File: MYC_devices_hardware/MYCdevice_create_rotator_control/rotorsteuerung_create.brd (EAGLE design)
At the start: 76.2 x 54.3 mm, 52 parts, among them IC1 MEGA8-P, IC3 7805T, K1 RT424012, K2 RT424012, K3 RT424012, Q1 20MHz, T1 BC547, T2 BC547, T3 BC547

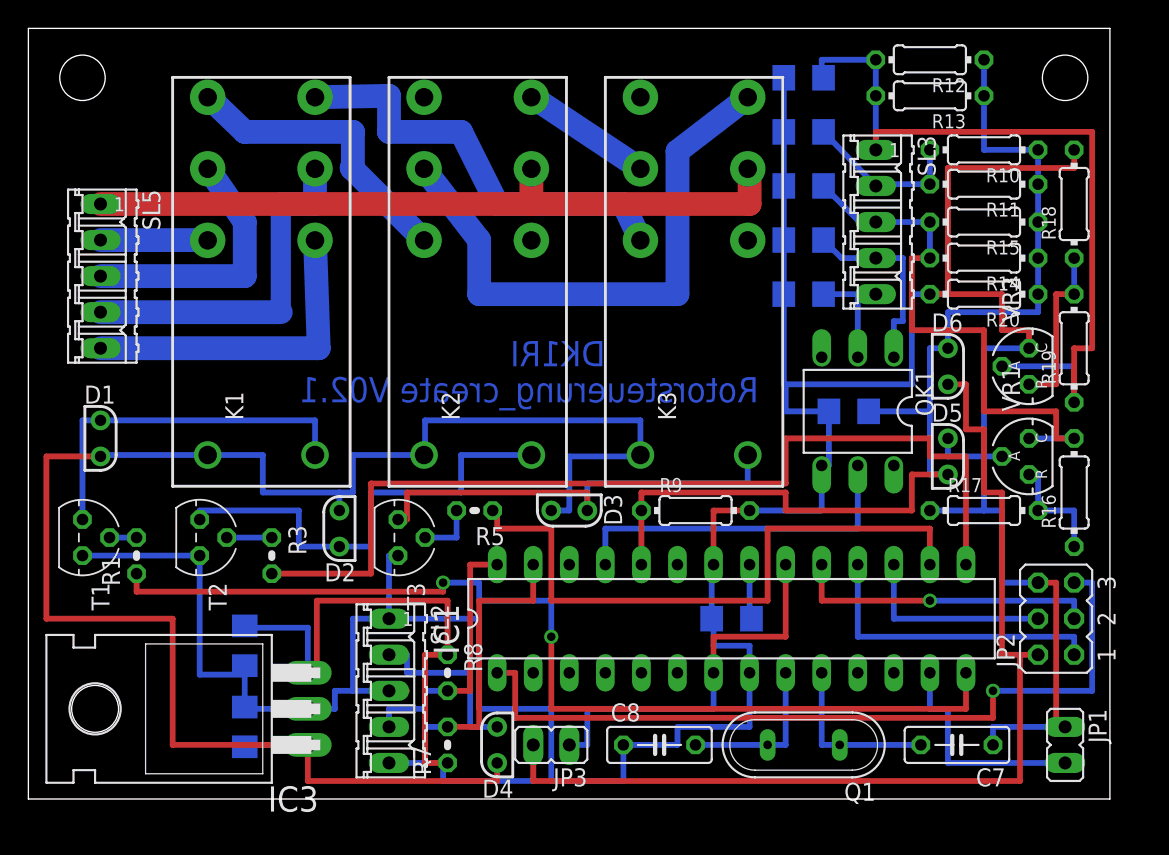
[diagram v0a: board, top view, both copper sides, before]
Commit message: new board. firmware with correction of nonlinearity and other
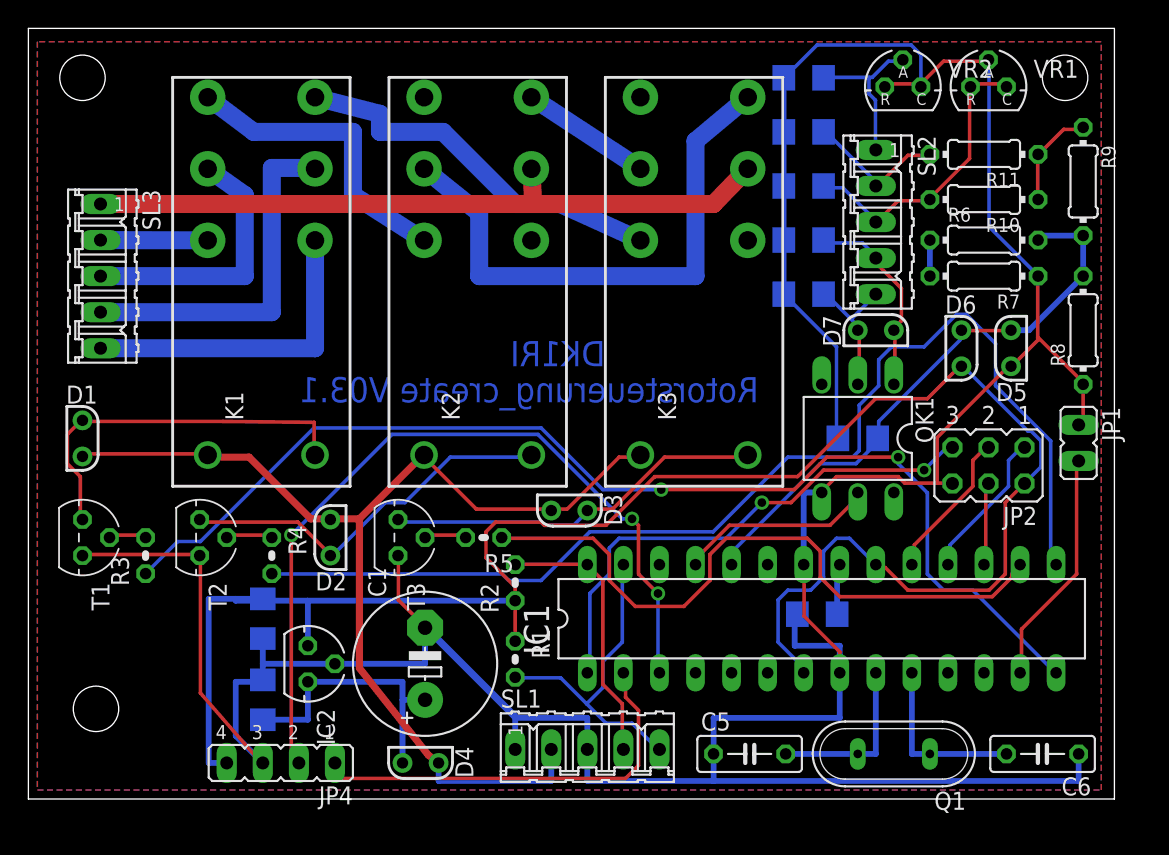
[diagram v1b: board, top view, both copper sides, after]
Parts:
- removed C13, C14, C15: 22u, resistor:C1206
- removed IC3: 7805T, linear:TO220H
- removed JP3: Power, jumper:JP1
- removed R12: 15k 1%, rcl:0204/7
- removed R13, R16, R18: 82k, rcl:0204/7
- removed R14: 7,5, rcl:0204/7
- removed R15: 47, rcl:0204/7
- removed R17, R19: 47k, rcl:0204/7
- removed R20: 220k, rcl:0204/7
- removed SL5: Motor, con-amp-quick:05P
- added C2, C3: 22u, resistor:C1206
- added C5, C6: 18pF, resistor:C050-025X075
- added D7: 1N4004, zetex:E2LINE
- added IC2: 78L05, v-reg:78LXX
- added JP4: USB, jumper:JP4
- added R2: 4k7, resistor:0204V
- added R4: 3.3k, resistor:0204V
- added R6: Ry, rcl:0204/7
- added SL1: I2C, con-amp-quick:05P
- C1: value 22u -> 1000u16V; device resistor:C1206 -> rcl:E5-10,5
- C7, C8: value 18pF -> 22u; device resistor:C050-025X075 -> resistor:C1206
- R1: value 3.3k -> 4k7
- R10: value 10k 1% -> 220k
- R11: value 1000M -> 220k
- R7, R8: value 4k7 -> Ry; device resistor:0204V -> rcl:0204/7
- R9: value 220k -> 75k
- SL2: value I2C -> Poti
- SL3: value Poti -> Motor
- moved SL3 54.7 mm to (5.08, 63.5)
- moved R8 50.9 mm to (74.3, 59.7), turned to 90 degrees
- moved R7 50.2 mm to (67.3, 63.5), turned to 180 degrees
- moved SL2 47.6 mm to (59.7, 67.3)
- moved C4 40.4 mm to (55.6, 39.7), turned to 180 degrees
- moved C7 37.2 mm to (54.6, 66.0), flipped to the bottom
- moved R9 35.8 mm to (74.3, 70.2), turned to 270 degrees
- moved C8 33.3 mm to (54.6, 62.2), flipped to the bottom, turned to 180 degrees
- moved C9 30.9 mm to (54.6, 69.8)
- moved R1 27.7 mm to (34.3, 36.5), turned to 270 degrees
- moved VR1 26.2 mm to (67.6, 76.8), turned to 0 degrees
- moved VR2 21.6 mm to (61.6, 76.8), turned to 0 degrees
- moved JP1 21.3 mm to (74.0, 51.8)
- moved C12 18.2 mm to (58.4, 52.1), turned to 0 degrees
- moved C11 15.2 mm to (54.6, 77.5)
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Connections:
- removed net N$11: K1.11, SL5.4
- removed net N$18: K2.11, K3.11, SL5.1
- removed net N$21: C15.1, D5.1, D6.2, IC1.24, R10.1, R11.1, R12.1, R13.1, R14.1, R15.1, R20.1, R9.1
- removed net N$24: C1.1, D1.1, D2.1, D3.1, D4.2, IC3.1, K1.A2, K2.A2, K3.A2
- removed net N$27: C12.2, R14.2, R15.2, R16.2, SL3.3, VR1.C
- removed net N$29: IC1.20, IC1.7, JP3.1
- removed net N$39: R16.1, R17.2, VR1.R
- removed net N$44: R18.1, R19.2, VR2.R
- new net C7: C7.2, D7.1, OK1.1, SL2.4
- new net C9: C9.2, R10.2, SL2.3, VR1.C, VR1.R
- new net CCW: K1.22, SL3.2
- new net CW: K1.12, SL3.5
- new net N$30: IC1.2, JP4.1
- new net N$32: IC1.3, JP4.2
- new net TO1: K2.11, K3.11, SL3.1
- new net TO2: K1.11, SL3.4
- new net TO3: K1.21, SL3.3
- net GND: now also C1.-, C12.2, C2.2, C3.2, C4.1, C5.1, C6.1, IC2.GND, JP4.3, R7.1, R8.1, SL1.1, SL1.3, VR2.R; no longer C1.2, C12.1, C13.1, C14.1, C15.2, C4.2, IC3.2, R17.1, R18.2, R20.2, R9.2, SL2.1, SL2.3
- net N$1: now also R1.2, SL1.5; no longer R7.2, SL2.5
- net N$10: now also R10.1, R11.1, R9.1; no longer K1.22, SL5.2
- net N$13: now also R4.1; no longer R3.1
- net N$17: now also C12.1, D5.1, D6.2, IC1.24, R6.2, R8.2, R9.2; no longer K1.12, SL5.5
- net N$19: now also C5.2; no longer C8.2
- net N$2: now also C1.+, C2.1, D4.1, IC2.IN; no longer K1.21, SL5.3
- net N$22: now also R4.2; no longer R3.2
- net N$25: now also D1.1, D2.1, D3.1, D4.2, K1.A2, K2.A2, K3.A2, SL1.2; no longer D4.1, SL2.2
- net N$28: now also C10.2, SL2.2; no longer C13.2, R10.2, SL3.2
- net N$3: now also C8.2, D7.2, SL2.5; no longer C11.2, SL3.5
- net N$33: now also R3.1; no longer R1.1
- net N$34: now also R3.2; no longer R1.2
- net N$35: now also C4.2; no longer C9.2
- net N$37: now also C6.2; no longer C7.2
- net N$4: now also C11.2, SL2.1; no longer C14.2, R12.2, R13.2, R19.1, SL3.1
- net N$5: now also R2.2, SL1.4; no longer R8.2, SL2.4
- net N$7: now also R6.1, R7.2; no longer C10.2, OK1.1, SL3.4
- net VDD: now also C3.1, IC1.20, IC1.7, IC2.OUT, JP4.4, R1.1, R2.1; no longer C4.1, IC3.3, JP3.2, R7.1, R8.1
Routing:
- net N$24: track 124.5 -> 0.00 mm
- net N$21: track 76.7 -> 0.00 mm
- net N$25: track 12.7 -> 77.2 mm
- net N$32: track 0.00 -> 57.3 mm, vias 0 -> 3
- net N$18: track 50.9 -> 0.00 mm
- net TO1: track 0.00 -> 49.1 mm
- net N$4: track 56.0 -> 11.4 mm
- net N$27: track 39.7 -> 0.00 mm
- net N$30: track 0.00 -> 29.6 mm
- net N$29: track 27.9 -> 0.00 mm
- net TO2: track 0.00 -> 25.3 mm
- net N$11: track 25.2 -> 0.00 mm
- net CW: track 0.00 -> 22.7 mm
- net C9: track 0.00 -> 21.1 mm
- net N$38: track 55.9 -> 36.6 mm, vias 1 -> 2
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- added copper zone on layer 1, net GND
- added copper zone on layer 16, net GND
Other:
- board size 76.2 x 54.3 mm -> 76.5 x 54.3 mm
- board text added: "Rotorsteuerung_create V03.1"
- board text removed: "Rotorsteuerung_create V02.1"

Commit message: new board and slavecore1.7
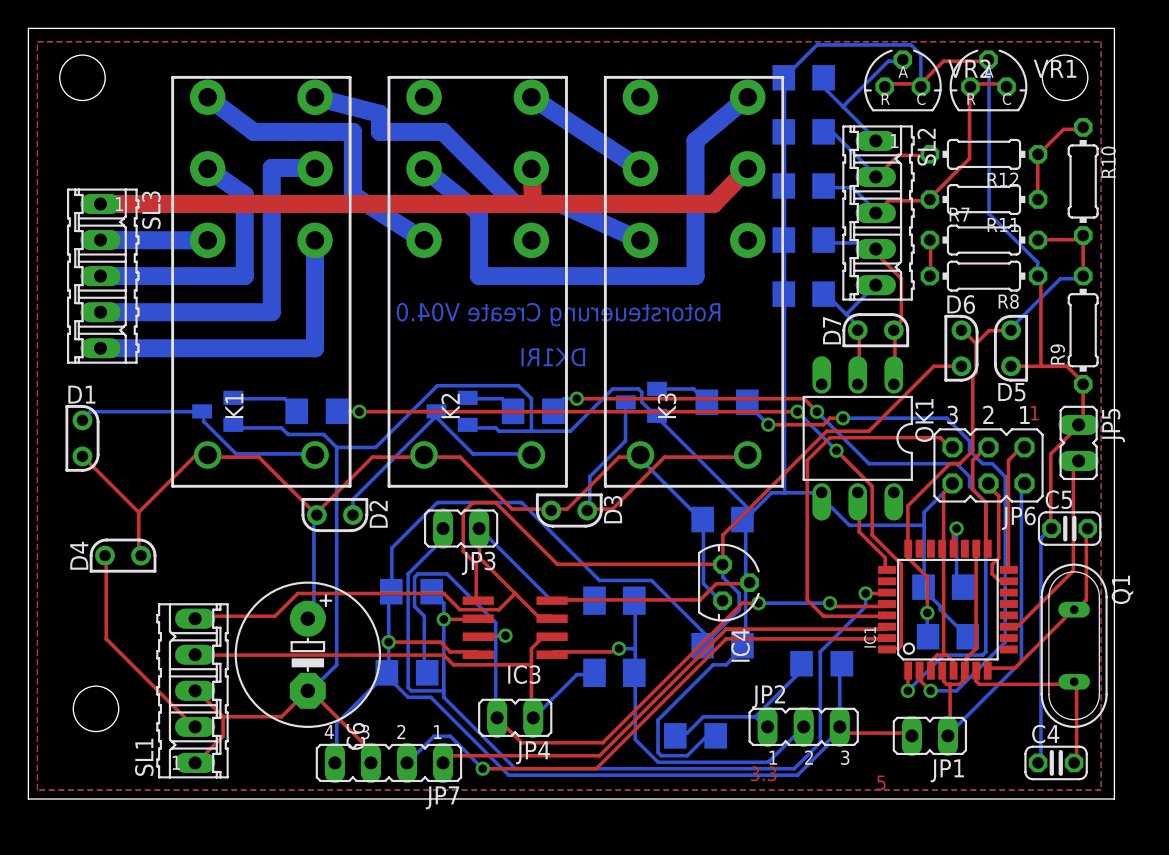
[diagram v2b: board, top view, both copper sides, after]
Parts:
- removed IC2: 78L05, v-reg:78LXX
- added IC3: PCA9517, PCA9517:SO-08
- added IC4: 78L05, v-reg:78LXX
- added JP3: SDA, jumper:JP1
- added JP5: Reset, jumper:JP1
- added JP6: ISP, jumper:JP3Q
- added JP7: USB, jumper:JP4
- added R12: 220k, rcl:0204/7
- added R31, R41, R51: 3.3k, resistor:R1206
- C1: value 1000u16V -> 22u; device rcl:E5-10,5 -> resistor:C1206
- C4: value 22u -> 18pF; device resistor:C1206 -> resistor:C025-024X044
- C5: device resistor:C050-025X075 -> resistor:C025-024X044
- C6: value 18pF -> 470u16V; device resistor:C050-025X075 -> rcl:E5-10,5
- IC1: value MEGA8-P -> MEGA8-AI; device atmel:DIL28-3 -> atmel:TQFP32-08
- JP1: value Reset -> Power
- JP2: value ISP -> 3,3V/5V; device jumper:JP3Q -> jumper:JP2
- JP4: value USB -> SCL; device jumper:JP4 -> jumper:JP1
- R1, R2: value 4k7 -> see manual; device resistor:0204V -> resistor:M1206
- R10: value 220k -> 75k
- R3, R4: value 3.3k -> see manual; device resistor:0204V -> resistor:R1206
- R5: value 3.3k -> 1k; device resistor:0204V -> resistor:R1206
- R6: value Ry -> 1k5; device rcl:0204/7 -> resistor:R1206
- R9: value 75k -> Ry
- T1, T2, T3: value BC547 -> (none); device transistor:TO92 -> transistor:SOT23-BEC
- moved C6 52.2 mm to (19.7, 36.8), turned to 270 degrees
- moved C3 48.0 mm to (64.5, 41.6), turned to 180 degrees
- moved R6 40.4 mm to (47.0, 31.1), flipped to the bottom
- moved C2 32.6 mm to (48.9, 37.5), turned to 180 degrees
- moved SL1 27.9 mm to (11.7, 34.3), turned to 90 degrees
- moved C5 27.6 mm to (73.3, 45.7)
- moved D4 25.5 mm to (6.67, 43.8), turned to 90 degrees
- moved R5 25.4 mm to (55.9, 36.2), flipped to the bottom
- moved C1 23.3 mm to (48.9, 46.4), flipped to the bottom, turned to 180 degrees
- moved JP1 23.1 mm to (63.5, 31.1), turned to 90 degrees
- moved JP2 22.6 mm to (54.6, 31.8), turned to 0 degrees
- moved R3 20.2 mm to (26.7, 35.6), flipped to the bottom, turned to 180 degrees
- moved T2 19.9 mm to (29.8, 54.0), flipped to the bottom
- moved C4 19.8 mm to (72.4, 29.2), flipped to the top, turned to 0 degrees
- moved T3 19.6 mm to (43.2, 54.6), flipped to the bottom
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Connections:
- removed net N$2: C1.+, C2.1, D4.1, IC2.IN
- new net N$11: IC1.18, IC1.4, IC1.6, JP1.1, JP6.2
- new net N$18: JP2.1, R5.1, R6.2
- new net N$24: IC3.3, JP3.1, R1.2, SL1.5
- new net N$27: IC3.2, JP4.1, R2.2, SL1.4
- new net N$29: IC3.1, JP2.2, R1.1, R2.1
- new net N$44: IC1.28, IC3.7, JP4.2, R3.2
- net C9: now also R11.2; no longer R10.2
- net GND: now also C1.2, C3.1, C6.-, IC1.21, IC1.3, IC1.5, IC3.4, IC4.GND, JP5.1, JP6.6, JP7.3, R6.1, R9.1, T1.E, T2.E, T3.E; no longer C1.-, C3.2, C6.1, IC1.22, IC1.8, IC2.GND, JP1.1, JP2.6, JP4.3, R7.1, T1.1, T2.1, T3.1
- net N$1: now also IC3.6, JP3.2, R4.2; no longer R1.2, SL1.5
- net N$10: now also R12.1; no longer R9.1
- net N$13: now also R41.1, T2.B; no longer R4.1, T2.2
- net N$15: now also IC1.2, R51.1; no longer IC1.16, R5.1
- net N$17: now also R10.2, R7.2; no longer R6.2, R8.2
- net N$19: now also C4.2, IC1.7; no longer C5.2, IC1.9
- net N$20: now also IC1.17, JP6.3; no longer IC1.19, JP2.3
- net N$22: now also IC1.1, R41.2; no longer IC1.15, R4.2
- net N$25: now also C1.1, C6.+, D4.1, IC4.IN; no longer D4.2, SL1.2
- net N$26: now also IC1.11, JP5.2; no longer IC1.13, JP1.2
- net N$28: now also R12.2; no longer R11.2
- net N$30: now also IC1.30, JP7.1; no longer IC1.2, JP4.1
- net N$31: now also IC1.15, JP6.4; no longer IC1.17, JP2.4
- net N$32: now also IC1.31, JP7.2; no longer IC1.3, JP4.2
- net N$33: now also IC1.32, R31.1; no longer IC1.14, R3.1
- net N$34: now also R31.2, T1.B; no longer R3.2, T1.2
- net N$35: now also C3.2, IC1.20; no longer C4.2, IC1.21
- net N$36: now also R51.2, T3.B; no longer R5.2, T3.2
- net N$37: now also C5.2, IC1.8; no longer C6.2, IC1.10
- net N$38: now also IC1.29, JP6.5; no longer IC1.1, JP2.5
- net N$40: now also T1.C; no longer T1.3
- net N$41: now also T2.C; no longer T2.3
- net N$42: now also T3.C; no longer T3.3
- net N$5: now also D4.2, SL1.2; no longer IC1.28, R2.2, SL1.4
- net N$7: now also R7.1, R8.2; no longer R6.1, R7.2
- net N$8: now also IC1.16, JP6.1; no longer IC1.18, JP2.1
- net VDD: now also C2.1, IC3.5, IC3.8, IC4.OUT, JP1.2, JP2.3, JP7.4, R3.1, R4.1, R5.2; no longer C3.1, IC1.20, IC1.7, IC2.OUT, JP2.2, JP4.4, R1.1, R2.1
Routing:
- net N$44: track 0.00 -> 56.2 mm, vias 0 -> 3
- net N$1: track 23.1 -> 67.9 mm, vias 0 -> 2
- net N$24: track 0.00 -> 43.5 mm
- net N$27: track 0.00 -> 36.4 mm
- net N$11: track 0.00 -> 35.8 mm
- net N$29: track 0.00 -> 29.5 mm, vias 0 -> 1
- net GND: track 253.1 -> 282.0 mm
- net N$33: track 81.0 -> 53.1 mm, vias 2 -> 3
- net N$22: track 80.2 -> 52.9 mm, vias 0 -> 3
- net VDD: track 131.7 -> 156.8 mm, vias 0 -> 1
- net N$2: track 19.8 -> 0.00 mm
- net N$32: track 57.3 -> 39.3 mm, vias 3 -> 1
- net N$18: track 0.00 -> 12.4 mm
- net N$38: track 36.6 -> 27.1 mm, vias 2 -> 0
- net N$41: track 27.4 -> 18.0 mm
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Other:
- board text added: "1"
- board text added: "3.3"
- board text added: "5"
- board text added: "Rotorsteuerung Create V04.0"
- board text removed: "Rotorsteuerung_create V03.1"
